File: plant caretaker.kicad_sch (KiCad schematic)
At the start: 2 parts, among them U4 ESP32-C3, U6 ESP32-C3-MINI-1-N4

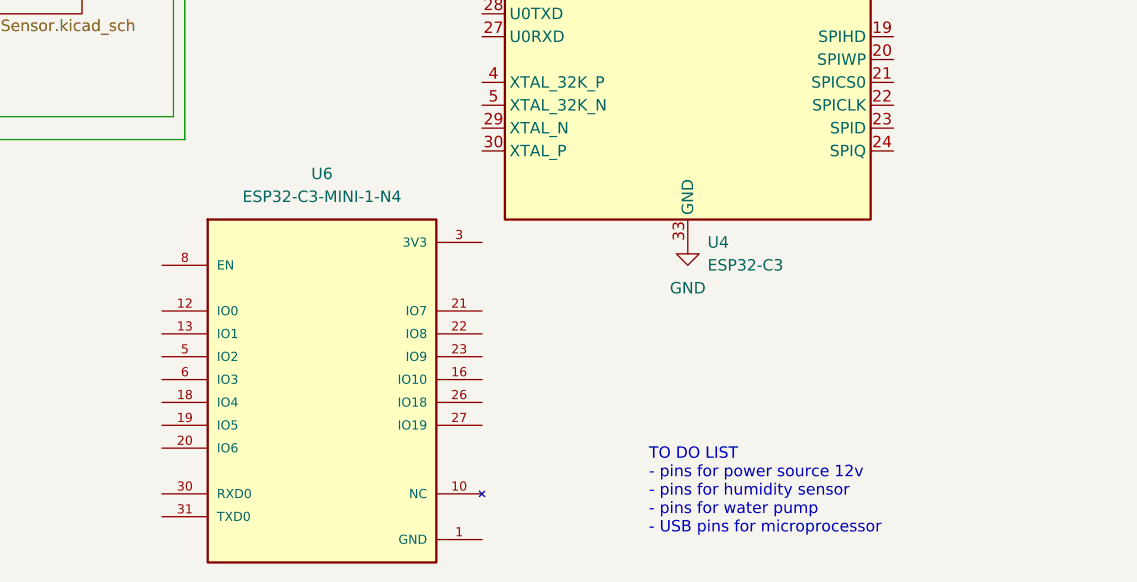
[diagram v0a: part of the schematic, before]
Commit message: Deleted ESP32
Will make manually the symbol
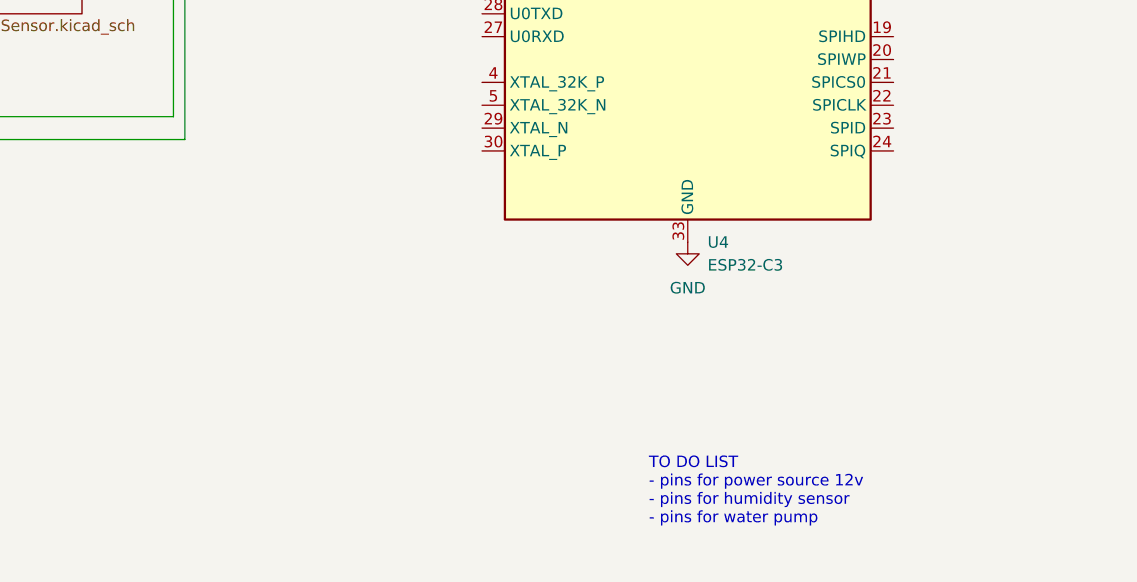
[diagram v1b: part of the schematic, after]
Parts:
- removed U6: ESP32-C3-MINI-1-N4, a, symbol ESP32-C3-MINI-1-N4:ESP32-C3-MINI-1-N4
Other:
- note added: "TO DO LIST - pins for power source 12v - pins for humidity sensor - pins for water pump"
- note removed: "TO DO LIST - pins for power source 12v - pins for humidity sensor - pins for water pump - USB pins for microprocessor"
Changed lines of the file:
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@@
 		)
 	)
-	(text "TO DO LIST\n- pins for power source 12v\n- pins for humidity sensor\n- pins for water pump\n- USB pins for microprocessor"
+	(text "TO DO LIST\n- pins for power source 12v\n- pins for humidity sensor\n- pins for water pump\n"
 		(exclude_from_sim no)
 		(at 195.072 145.796 0)
@@
 					(unit 1)
 				)
-			)
-		)
-	)
-	(symbol
-		(lib_id "ESP32-C3-MINI-1-N4:ESP32-C3-MINI-1-N4")
-		(at 158.75 133.35 0)
-		(unit 1)
-		(exclude_from_sim no)
-		(in_bom yes)
-		(on_board yes)
-		(dnp no)
-		(fields_autoplaced yes)
-		(property "Reference" "U6"
-			(at 158.75 110.49 0)
-			(effects
-				(font
-					(size 1.27 1.27)
-				)
-			)
-		)
-		(property "Value" "ESP32-C3-MINI-1-N4"
-			(at 158.75 113.03 0)
-			(effects
-				(font
-					(size 1.27 1.27)
-				)
-			)
-		)
-		(property "Footprint" "a"
-			(at 158.75 133.35 0)
-			(effects
-				(font
-					(size 1.27 1.27)
-				)
-				(justify bottom)
-				(hide yes)
-			)
-		)
-		(property "Datasheet" ""
-			(at 158.75 133.35 0)
-			(effects
-				(font
-					(size 1.27 1.27)
-				)
-				(hide yes)
-			)
-		)
-		(property "Description" ""
-			(at 158.75 133.35 0)
-			(effects
-				(font
-					(size 1.27 1.27)
-				)
-				(hide yes)
-			)
-		)
-		(property "MF" "a"
-			(at 158.75 133.35 0)
-			(effects
-				(font
-					(size 1.27 1.27)
-				)
-				(justify bottom)
-				(hide yes)
-			)
-		)
-		(property "MAXIMUM_PACKAGE_HEIGHT" "a"
-			(at 158.75 133.35 0)
-			(effects
-				(font
-					(size 1.27 1.27)
-				)
-				(justify bottom)
-				(hide yes)
-			)
-		)
-		(property "Package" "a"
-			(at 158.75 133.35 0)
-			(effects
-				(font
-					(size 1.27 1.27)
-				)
-				(justify bottom)
-				(hide yes)
-			)
-		)
-		(property "Price" "a"
-			(at 158.75 133.35 0)
-			(effects
-				(font
-					(size 1.27 1.27)
-				)
-				(justify bottom)
-				(hide yes)
-			)
-		)
-		(property "Check_prices" "a"
-			(at 158.75 133.35 0)
-			(effects
-				(font
-					(size 1.27 1.27)
-				)
-				(justify bottom)
-				(hide yes)
-			)
-		)
-		(property "STANDARD" "a"
-			(at 158.75 133.35 0)
-			(effects
-				(font
-					(size 1.27 1.27)
-				)
-				(justify bottom)
-				(hide yes)
-			)
-		)
-		(property "PARTREV" "a"
-			(at 158.75 133.35 0)
-			(effects
-				(font
-					(size 1.27 1.27)
-				)
-				(justify bottom)
-				(hide yes)
-			)
-		)
-		(property "SnapEDA_Link" "a"
-			(at 158.75 133.35 0)
-			(effects
-				(font
-					(size 1.27 1.27)
-				)
-				(justify bottom)
-				(hide yes)
-			)
-		)
-		(property "MP" "a"
-			(at 158.75 133.35 0)
-			(effects
-				(font
-					(size 1.27 1.27)
-				)
-				(justify bottom)
-				(hide yes)
-			)
-		)
-		(property "Description_1" "a"
-			(at 158.75 133.35 0)
-			(effects
-				(font
-					(size 1.27 1.27)
-				)
-				(justify bottom)
-				(hide yes)
-			)
-		)
-		(property "Availability" "a"
-			(at 158.75 133.35 0)
-			(effects
-				(font
-					(size 1.27 1.27)
-				)
-				(justify bottom)
-				(hide yes)
-			)
-		)
-		(property "MANUFACTURER" "a"
-			(at 158.75 133.35 0)
-			(effects
-				(font
-					(size 1.27 1.27)
-				)
-				(justify bottom)
-				(hide yes)
-			)
-		)
-		(pin "19"
-		)
-		(pin "8"
-		)
-		(pin "6"
-		)
-		(pin "5"
-		)
-		(pin "20"
-		)
-		(pin "21"
-		)
-		(pin "26"
-		)
-		(pin "3"
-		)
-		(pin "22"
-		)
-		(pin "27"
-		)
-		(pin "31"
-		)
-		(pin "30"
-		)
-		(pin "23"
-		)
-		(pin "13"
-		)
-		(pin "10"
-		)
-		(pin "16"
-		)
-		(pin "12"
-		)
-		(pin "18"
-		)
-		(pin "1"
-		)
-		(instances
-			(project ""
-				(path "/23b35dcc-615e-4aec-abee-c26cc3d8b906"
-					(reference "U6")
-					(unit 1)
-				)

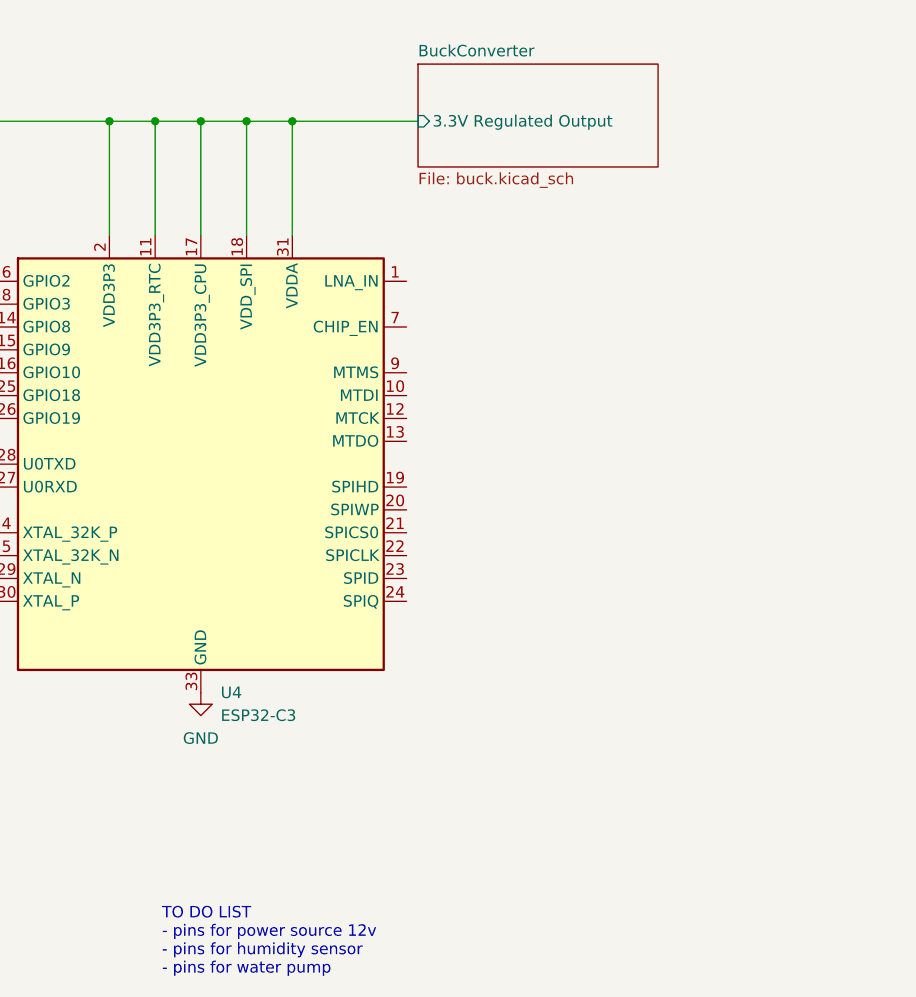
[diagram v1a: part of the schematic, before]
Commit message: Added a jack for power supply
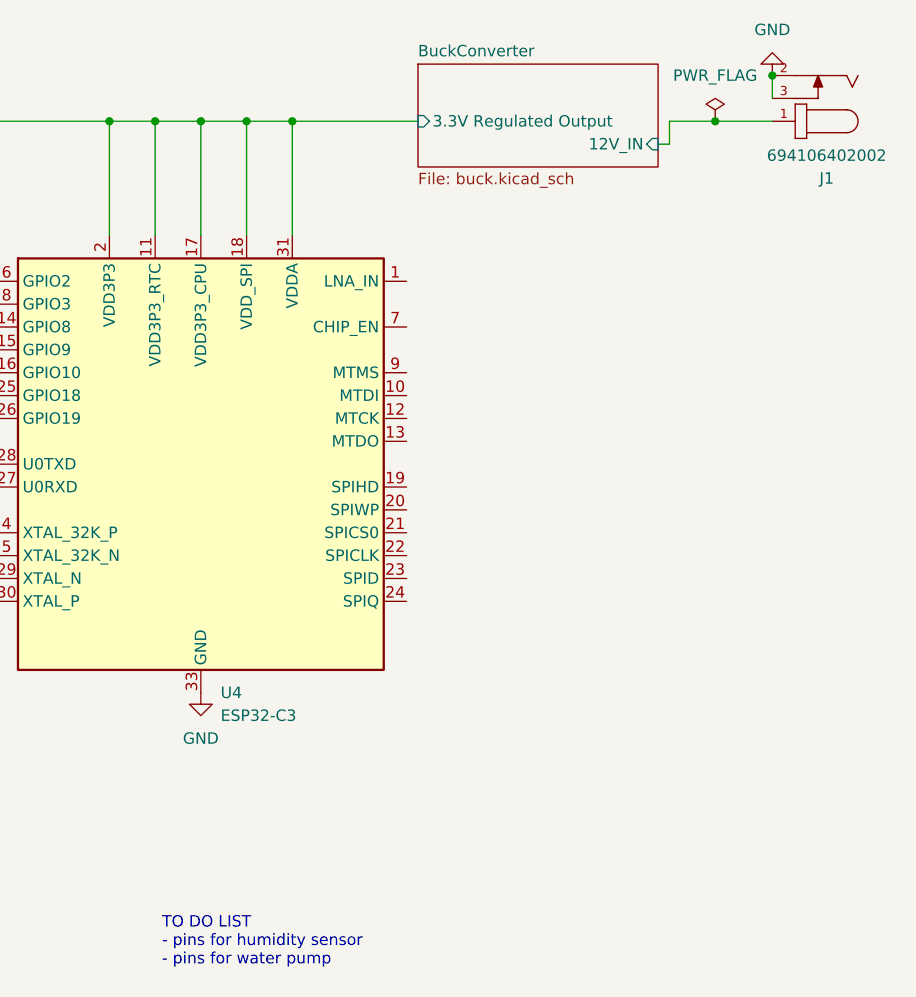
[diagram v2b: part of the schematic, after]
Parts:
- added J1: 694106402002, 694106402002:694106402002, symbol 694106402002:694106402002
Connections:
- net GND: now also J1.2, J1.3
- new net BuckConverter/12V_IN: J1.1
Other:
- sheet BuckConverter ports: added 12V_IN; removed none
- note added: "TO DO LIST - pins for humidity sensor - pins for water pump"
- note removed: "TO DO LIST - pins for power source 12v - pins for humidity sensor - pins for water pump"

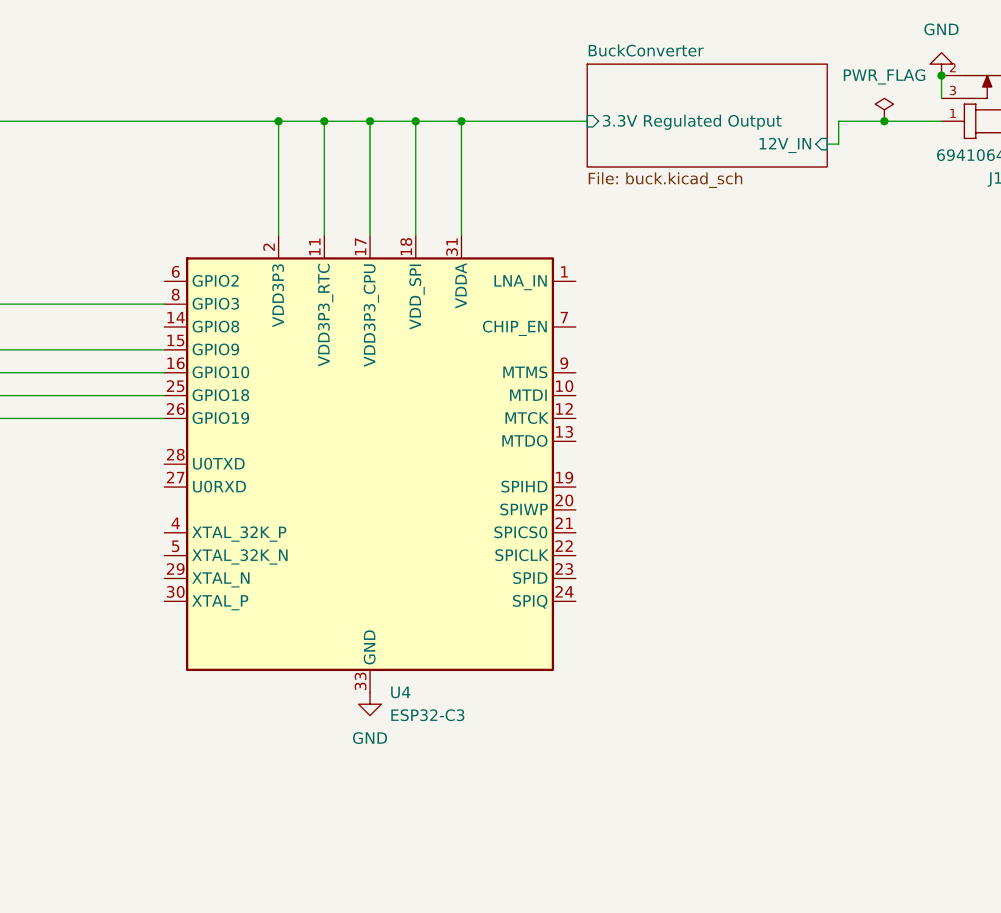
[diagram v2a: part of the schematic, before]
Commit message: Switched model of buck converter
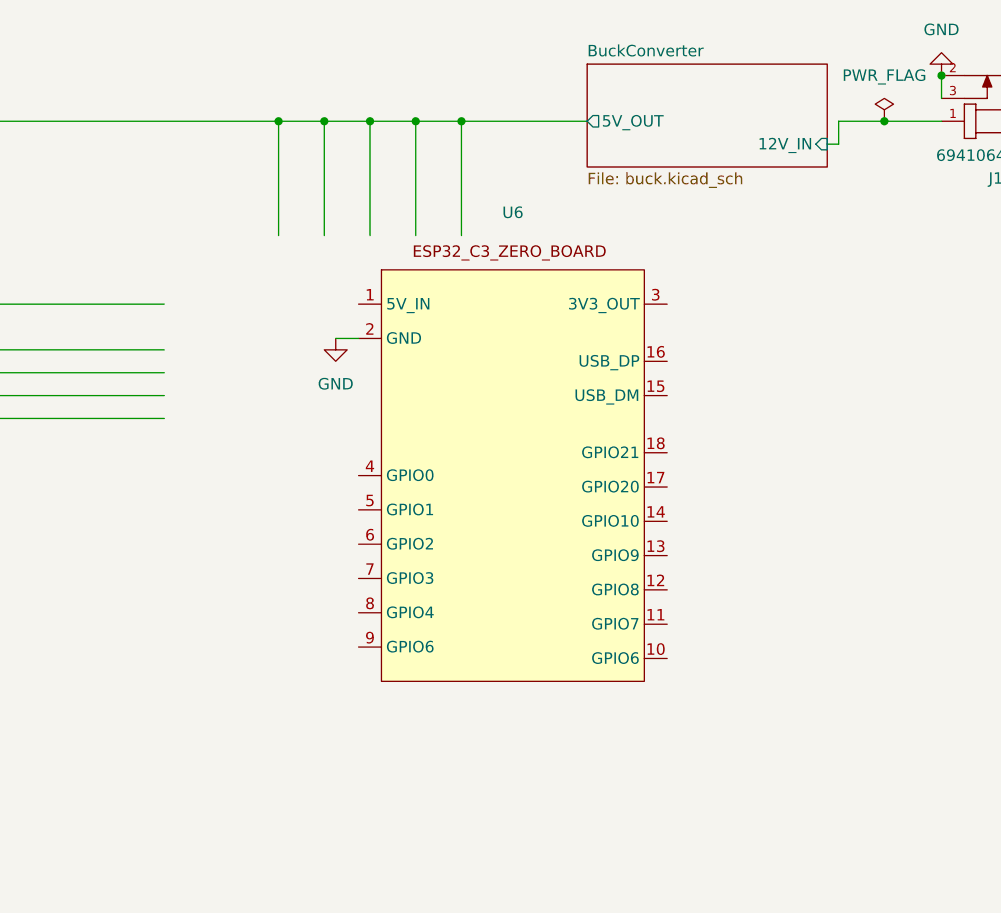
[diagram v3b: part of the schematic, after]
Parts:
- removed U4: ESP32-C3, Package_DFN_QFN:QFN-32-1EP_5x5mm_P0.5mm_EP3.7x3.7mm, symbol MCU_Espressif:ESP32-C3
- added U6: ~, symbol ESP32_C3_ZERO_Library:ESP32-C3-ZERO
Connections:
- net GND: now also U6.2 (GND)
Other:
- sheet BuckConverter ports: added 5V_OUT; removed 3.3V Regulated Output
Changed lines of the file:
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@@
+	(wire
+		(pts
+			(xy 195.58 78.74) (xy 198.12 78.74)
+		)
+		(stroke
+			(width 0)
+			(type default)
+		)
+	)
 	(wire
 		(pts
@@
 	)
 	(symbol
-		(lib_id "MCU_Espressif:ESP32-C3")
-		(at 199.39 92.71 0)
+		(lib_id "ESP32_C3_ZERO_Library:ESP32-C3-ZERO")
+		(at 214.63 95.25 0)
 		(unit 1)
 		(exclude_from_sim no)
@@
 		(dnp no)
 		(fields_autoplaced yes)
-		(property "Reference" "U4"
-			(at 201.5841 118.11 0)
-			(effects
-				(font
-					(size 1.27 1.27)
-				)
-				(justify left)
-			)
-		)
-		(property "Value" "ESP32-C3"
-			(at 201.5841 120.65 0)
-			(effects
-				(font
-					(size 1.27 1.27)
-				)
-				(justify left)
-			)
-		)
-		(property "Footprint" "Package_DFN_QFN:QFN-32-1EP_5x5mm_P0.5mm_EP3.7x3.7mm"
-			(at 199.898 92.71 0)
-			(effects
-				(font
-					(size 1.27 1.27)
-				)
-				(hide yes)
-			)
-		)
-		(property "Datasheet" "https://www.espressif.com/sites/default/files/documentation/esp32-c3_datasheet_en.pdf"
-			(at 199.898 92.71 0)
-			(effects
-				(font
-					(size 1.27 1.27)
-				)
-				(hide yes)
-			)
-		)
-		(property "Description" "RF Module, ESP32 SoC, RISC-V, WiFi 802.11b/n/g, Bluetooth LE 5, QFN32"
-			(at 199.898 92.71 0)
-			(effects
-				(font
-					(size 1.27 1.27)
-				)
-				(hide yes)
-			)
-		)
-		(pin "31"
-		)
-		(pin "21"
-		)
-		(pin "30"
+		(property "Reference" "U6"
+			(at 215.265 64.77 0)
+			(effects
+				(font
+					(size 1.27 1.27)
+				)
+			)
+		)
+		(property "Value" "~"
+			(at 215.265 66.04 0)
+			(effects
+				(font
+					(size 1.27 1.27)
+				)
+			)
+		)
+		(property "Footprint" ""
+			(at 207.01 91.44 0)
+			(effects
+				(font
+					(size 1.27 1.27)
+				)
+				(hide yes)
+			)
+		)
+		(property "Datasheet" ""
+			(at 207.01 91.44 0)
+			(effects
+				(font
+					(size 1.27 1.27)
+				)
+				(hide yes)
+			)
+		)
+		(property "Description" ""
+			(at 207.01 91.44 0)
+			(effects
+				(font
+					(size 1.27 1.27)
+				)
+				(hide yes)
+			)
+		)
+		(pin "14"
+		)
+		(pin "3"
+		)
+		(pin "15"
+		)
+		(pin "9"
+		)
+		(pin "10"
+		)
+		(pin "18"
+		)
+		(pin "11"
+		)
+		(pin "8"
 		)
 		(pin "1"
 		)
-		(pin "29"
-		)
-		(pin "3"
+		(pin "4"
+		)
+		(pin "12"
+		)
+		(pin "2"
+		)
+		(pin "5"
 		)
 		(pin "17"
 		)
-		(pin "5"
-		)
-		(pin "4"
-		)
-		(pin "8"
-		)
-		(pin "19"
-		)
-		(pin "9"
-		)
-		(pin "10"
-		)
-		(pin "27"
-		)
-		(pin "15"
-		)
-		(pin "12"
-		)
-		(pin "24"
-		)
-		(pin "14"
-		)
-		(pin "25"
-		)
-		(pin "26"
+		(pin "13"
+		)
+		(pin "16"
 		)
 		(pin "6"
 		)
-		(pin "22"
-		)
-		(pin "18"
-		)
-		(pin "28"
-		)
-		(pin "33"
-		)
-		(pin "23"
-		)
 		(pin "7"
 		)
-		(pin "13"
-		)
-		(pin "11"
-		)
-		(pin "20"
-		)
-		(pin "32"
-		)
-		(pin "2"
-		)
-		(pin "16"
-		)
 		(instances
-			(project "plant caretaker"
+			(project ""
 				(path "/23b35dcc-615e-4aec-abee-c26cc3d8b906"
-					(reference "U4")
+					(reference "U6")
 					(unit 1)
 				)
@@
 	(symbol
 		(lib_id "power:GND")
-		(at 199.39 118.11 0)
+		(at 195.58 78.74 0)
 		(unit 1)
 		(exclude_from_sim no)
@@
 		(fields_autoplaced yes)
 		(property "Reference" "#PWR036"
-			(at 199.39 124.46 0)
+			(at 195.58 85.09 0)
 			(effects
 				(font
@@
 		)
 		(property "Value" "GND"
-			(at 199.39 123.19 0)
+			(at 195.58 83.82 0)
 			(effects
 				(font
@@
 		)
 		(property "Footprint" ""
-			(at 199.39 118.11 0)
+			(at 195.58 78.74 0)
 			(effects
 				(font
@@
 		)
 		(property "Datasheet" ""
-			(at 199.39 118.11 0)
+			(at 195.58 78.74 0)
 			(effects
 				(font
@@
 		)
 		(property "Description" "Power symbol creates a global label with name \"GND\" , ground"
-			(at 199.39 118.11 0)
+			(at 195.58 78.74 0)
 			(effects
 				(font
@@
 			)
 		)
-		(pin "3.3V Regulated Output" input
-			(at 223.52 54.61 180)
-			(effects
-				(font
-					(size 1.27 1.27)
-				)
-				(justify left)
-			)
-		)
 		(pin "12V_IN" input
 			(at 250.19 57.15 0)
@@
 			)
 		)
+		(pin "5V_OUT" output
+			(at 223.52 54.61 180)
+			(effects
+				(font
+					(size 1.27 1.27)
+				)
+				(justify left)
+			)
+		)
